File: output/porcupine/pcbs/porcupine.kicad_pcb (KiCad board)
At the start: 2 copper layers, 165.2 x 103.2 mm, 70 parts, among them J1 Jumper, J2 Jumper

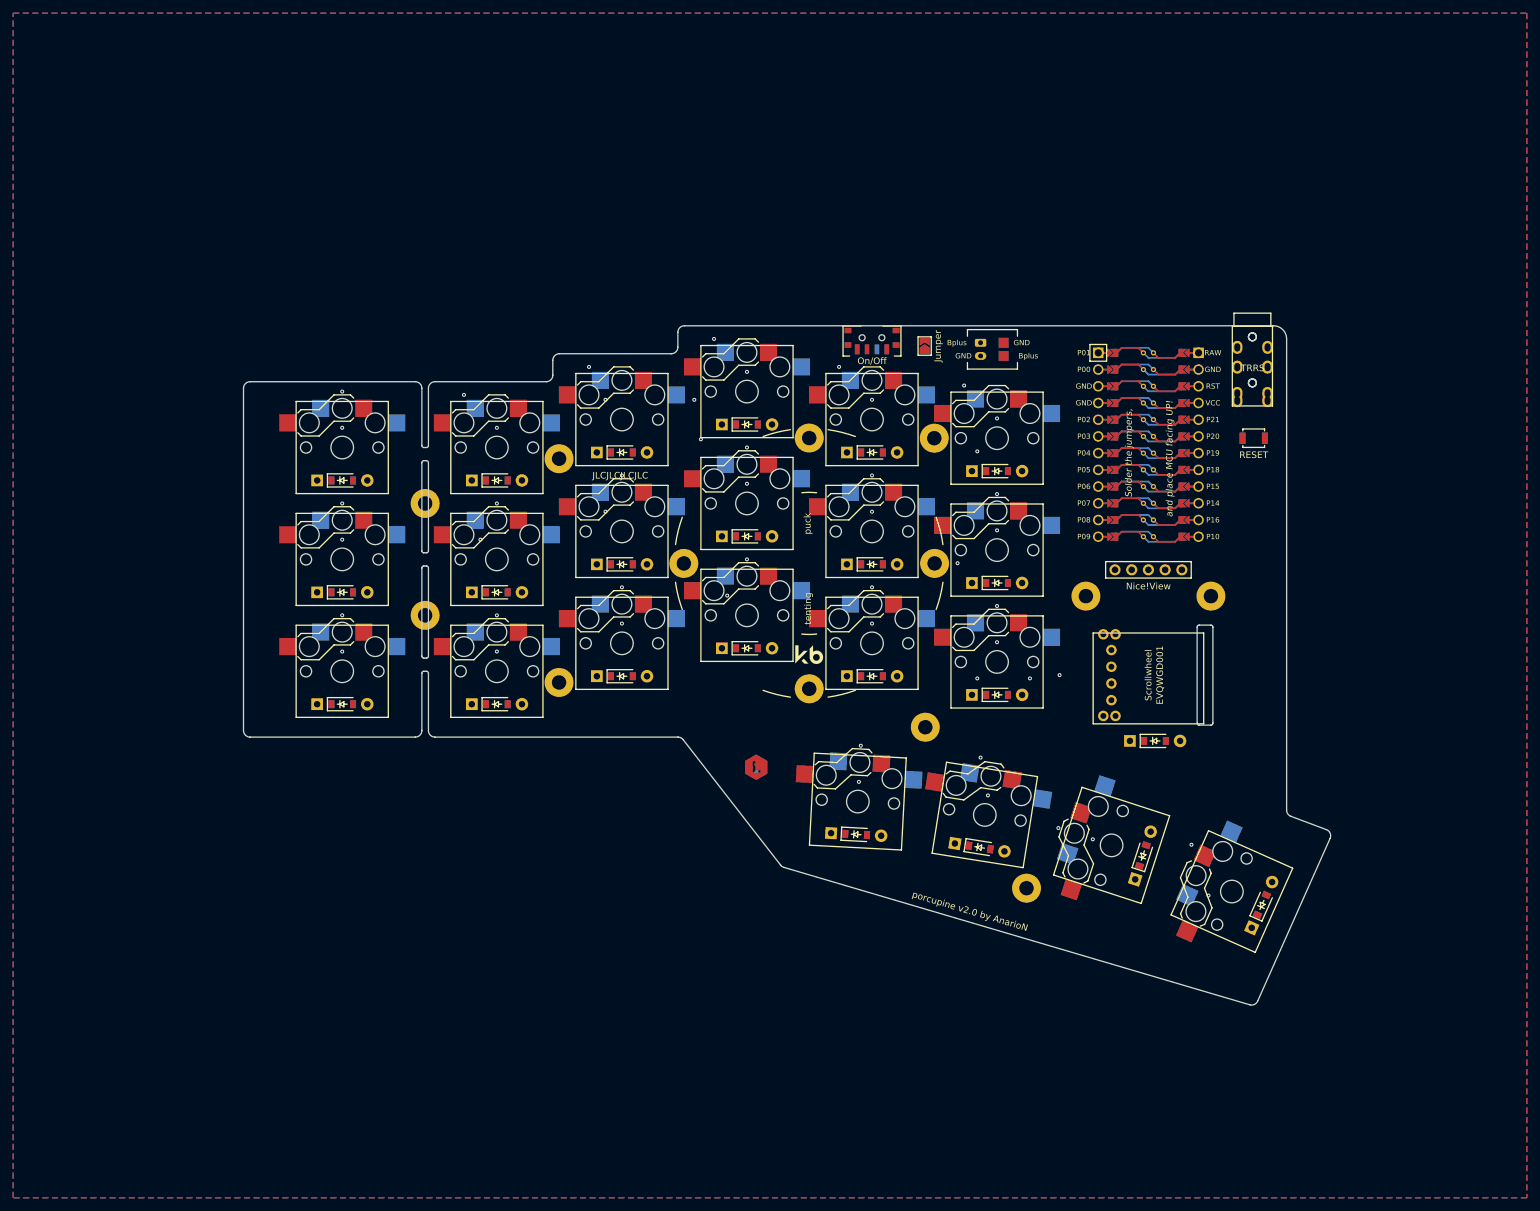
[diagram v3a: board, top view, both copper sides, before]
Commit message: Add images and cases
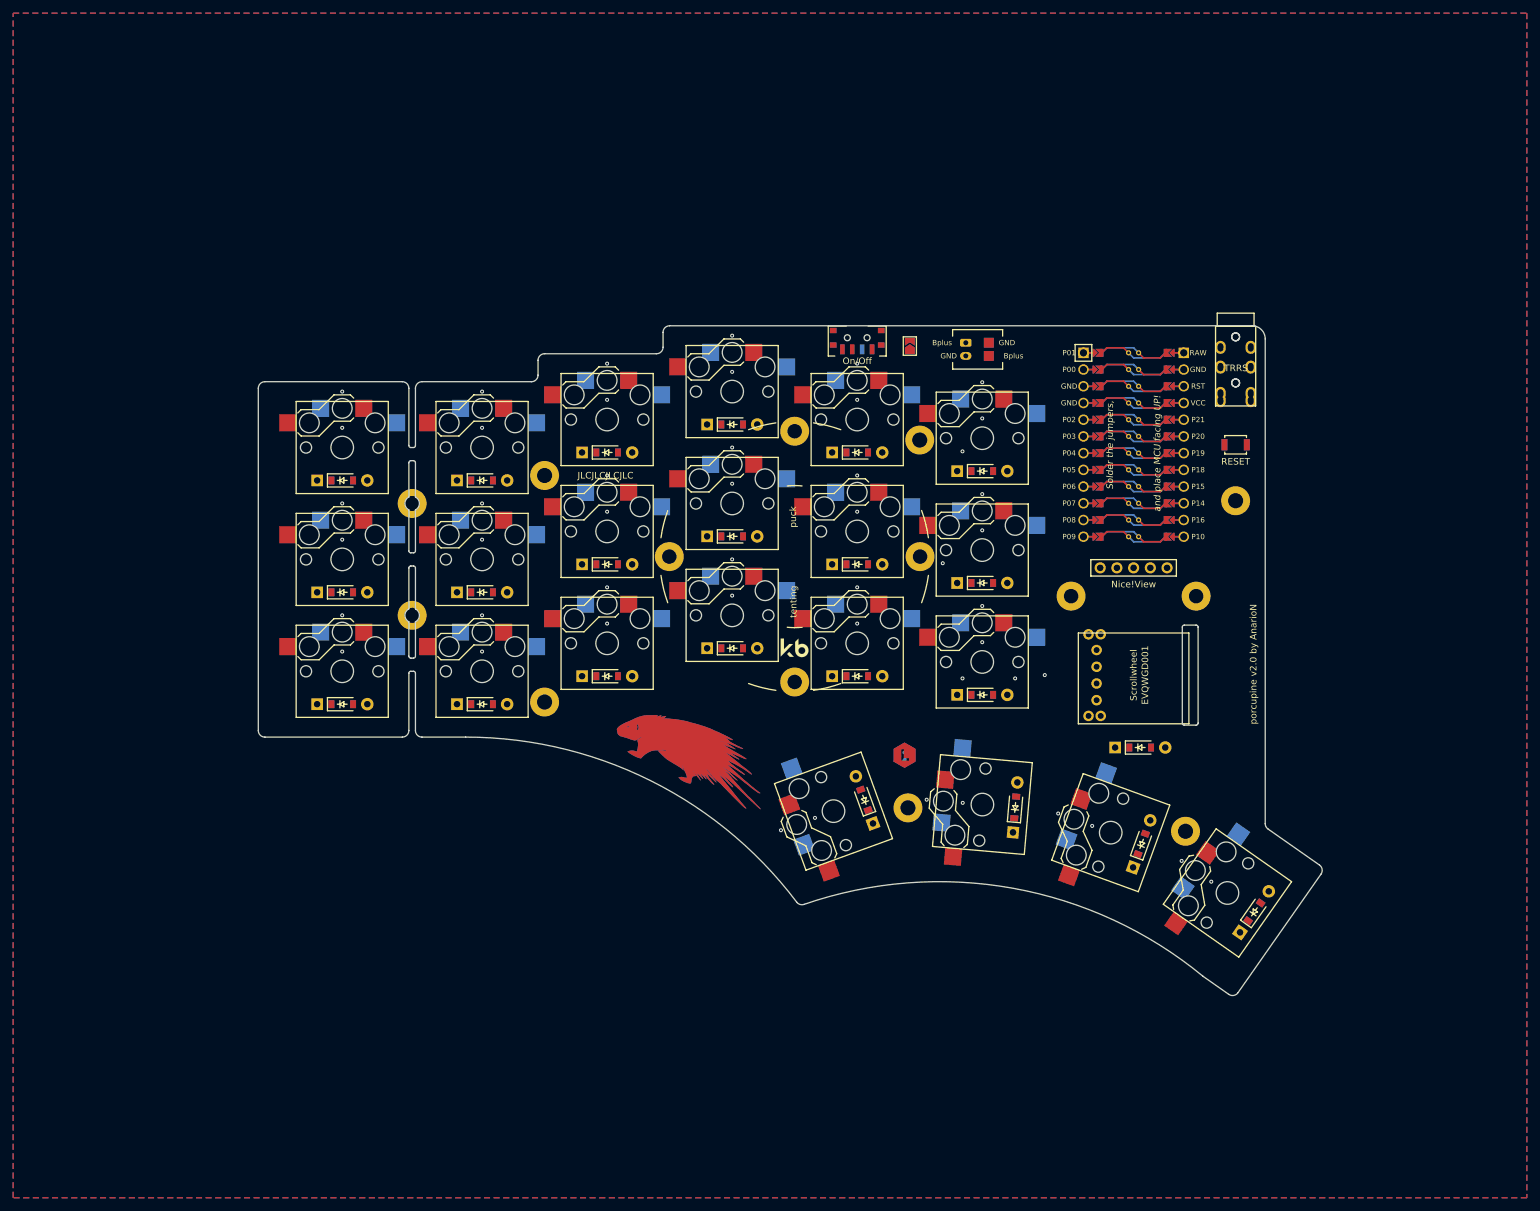
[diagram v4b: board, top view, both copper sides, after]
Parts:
- removed REF**: RollerEncoder_Panasonic_EVQWGD001, RollerEncoder_Panasonic_EVQWGD001
- removed _3: , Button_Switch_SMD:SW_SPDT_PCM12
- removed _4_B, _4_F: SW_Push, Button_Switch_SMD:SW_SPST_B3U-1000P
- removed _67, _68, _69, _70, _71, _72, _73, _74, _75: hole, Through Hole
- removed _7: Tenting Puck, Tenting Puck
- added H1: hole, Through Hole, F.Cu at (260.8, 138.6)
- added H10: hole, Through Hole, F.Cu at (278.1, 174.3)
- added H2: hole, Through Hole, F.Cu at (279.8, 138.6)
- added H3: hole, Through Hole, F.Cu at (160.6, 124.5)
- added H4: hole, Through Hole, F.Cu at (160.6, 141.5)
- added H5: hole, Through Hole, F.Cu at (180.8, 120.2)
- added H6: hole, Through Hole, F.Cu at (180.8, 154.7)
- added H7: hole, Through Hole, F.Cu at (237.8, 114.9)
- added H8: hole, Through Hole, F.Cu at (236.0, 170.8)
- added H9: hole, Through Hole, F.Cu at (285.8, 124.1)
- added LOGO_B: , Porcupine Logo, B.Cu at (203.8, 162.8)
- added LOGO_F: , Porcupine Logo, F.Cu at (203.8, 162.8)
- added RST1_B: SW_Push, Button_Switch_SMD:SW_SPST_B3U-1000P, B.Cu at (285.8, 115.6)
- added RST1_F: SW_Push, Button_Switch_SMD:SW_SPST_B3U-1000P, F.Cu at (285.8, 115.6)
- added S23: RollerEncoder_Panasonic_EVQWGD001, RollerEncoder_Panasonic_EVQWGD001, F.Cu at (270.2, 150.6)
- added SW1: , Button_Switch_SMD:SW_SPDT_PCM12, F.Cu at (228.2, 99.7)
- added TP1: Tenting Puck, Tenting Puck, F.Cu at (218.8, 132.6)
- moved Side_B 24.4 mm to (235.4, 162.8)
- moved Side_F 24.0 mm to (235.4, 162.8)
- moved D20 8.13 mm to (252.3, 170.7), turned to 85 degrees
- moved D19 5.40 mm to (229.3, 169.5), turned to 110 degrees
- moved S19 3.97 mm to (224.7, 171.2), turned to 110 degrees
- moved TRRS_B 2.55 mm to (285.8, 97.6)
- moved TRRS_F 2.55 mm to (285.8, 97.6)
- moved D23 2.46 mm to (271.2, 161.6)
- moved Nice!View1 2.27 mm to (270.2, 134.3)
- moved BAT1 2.25 mm to (244.8, 101.1)
- moved D16 2.25 mm to (247.2, 153.6)
- moved D17 2.25 mm to (247.2, 136.6)
- moved D18 2.25 mm to (247.2, 119.6)
- moved J1 2.25 mm to (236.2, 100.6)
- moved J2 2.25 mm to (236.2, 100.6)
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- renumbered _2 to BAT1
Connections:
- D1 pad 2: outer_bottom -> row_bottom
- D10 pad 2: middle_bottom -> row_bottom
- D11 pad 2: middle_home -> row_home
- D12 pad 2: middle_top -> row_top
- D13 pad 2: index_bottom -> row_bottom
- D14 pad 2: index_home -> row_home
- D15 pad 2: index_top -> row_top
- D16 pad 2: inner_bottom -> row_bottom
- D17 pad 2: inner_home -> row_home
- D18 pad 2: inner_top -> row_top
- D19 pad 2: inner_thumb -> row_thumb
- D2 pad 2: outer_home -> row_home
- D20 pad 2: near_thumb -> row_thumb
- D21 pad 2: home_thumb -> row_thumb
- D22 pad 2: far_thumb -> row_thumb
- D23 pad 1: inner_bottom -> scrollwheel_scrollwheel
- D23 pad 2: inner_bottom -> row_thumb
- D3 pad 2: outer_top -> row_top
- D4 pad 2: pinky_bottom -> row_bottom
- D5 pad 2: pinky_home -> row_home
- D6 pad 2: pinky_top -> row_top
- D7 pad 2: ring_bottom -> row_bottom
- D8 pad 2: ring_home -> row_home
- D9 pad 2: ring_top -> row_top
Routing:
- net GND: vias 7 -> 5
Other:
- board size 165.2 x 103.2 mm -> 161.7 x 101.8 mm
- net class Default added: clearance 0.2, trace_width 0.25, via_dia 0.8, via_drill 0.4
- net class Power added: clearance 0.2, trace_width 0.5, via_dia 0.8, via_drill 0.4

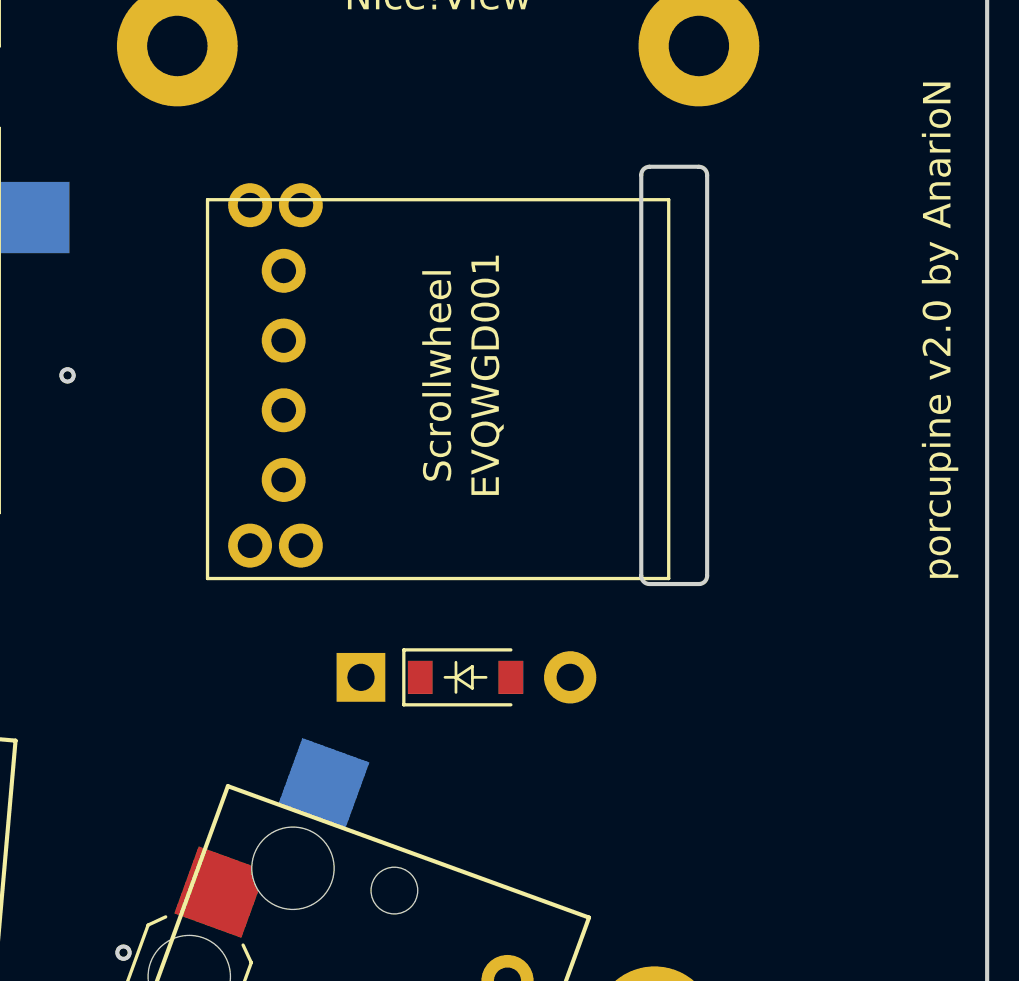
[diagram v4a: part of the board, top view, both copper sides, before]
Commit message: Add both horizontal and vertical scrollbar
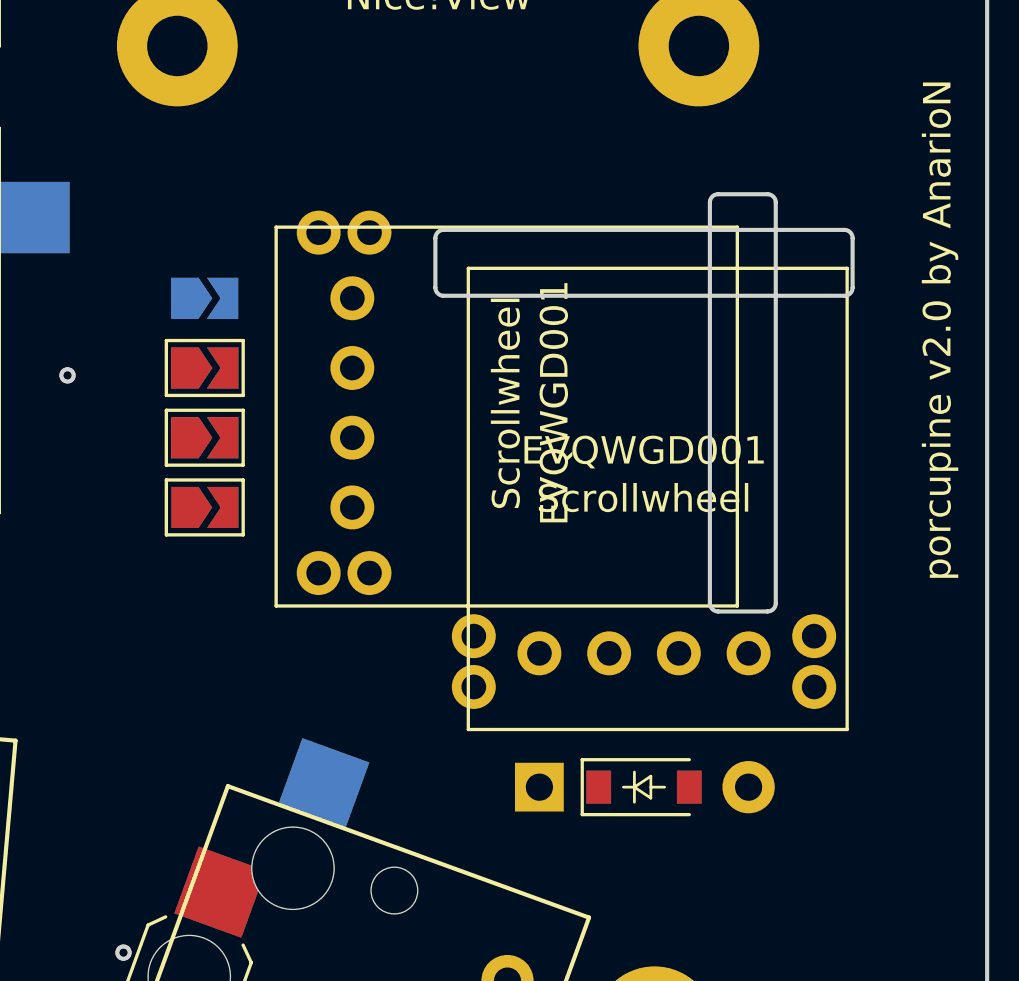
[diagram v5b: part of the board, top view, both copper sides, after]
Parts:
- added J3: Jumper, Jumper:SolderJumper-2_P1.3mm_Open_TrianglePad1.0x1.5mm, B.Cu at (261.8, 152.9)
- added J4: Jumper, Jumper:SolderJumper-2_P1.3mm_Open_TrianglePad1.0x1.5mm, F.Cu at (261.8, 155.4)
- added J5: Jumper, Jumper:SolderJumper-2_P1.3mm_Open_TrianglePad1.0x1.5mm, F.Cu at (261.8, 152.9)
- added J6: Jumper, Jumper:SolderJumper-2_P1.3mm_Open_TrianglePad1.0x1.5mm, F.Cu at (261.8, 150.3)
- added J7: Jumper, Jumper:SolderJumper-2_P1.3mm_Open_TrianglePad1.0x1.5mm, B.Cu at (236.2, 100.6)
- added J8: Jumper, Jumper:SolderJumper-2_P1.3mm_Open_TrianglePad1.0x1.5mm, F.Cu at (236.2, 100.6)
- added S24: RollerEncoder_Panasonic_EVQWGD001, RollerEncoder_Panasonic_EVQWGD001, F.Cu at (272.8, 151.6)
- J2: moved to B.Cu
- moved J2 55.9 mm to (261.8, 150.3), turned to 0 degrees
- moved J1 53.6 mm to (261.8, 147.8), turned to 0 degrees
- moved S23 8.75 mm to (277.8, 155.1), turned to 90 degrees
- moved D23 7.63 mm to (277.8, 165.6)
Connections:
- J1 pad 1: Bplus -> ENCB
- J1 pad 2: RAW -> ENCB_undef
- J2 pad 1: Bplus -> GND
- J2 pad 2: RAW -> GND_ENCA
- S23 pad A: ENCB -> ENCB_undef
- S23 pad B: GND -> GND_ENCA
- S23 pad C: ENCA -> ENCA_GND
- S23 pad D: undef -> undef_ENCB
